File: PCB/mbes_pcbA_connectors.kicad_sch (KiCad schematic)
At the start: 15 parts

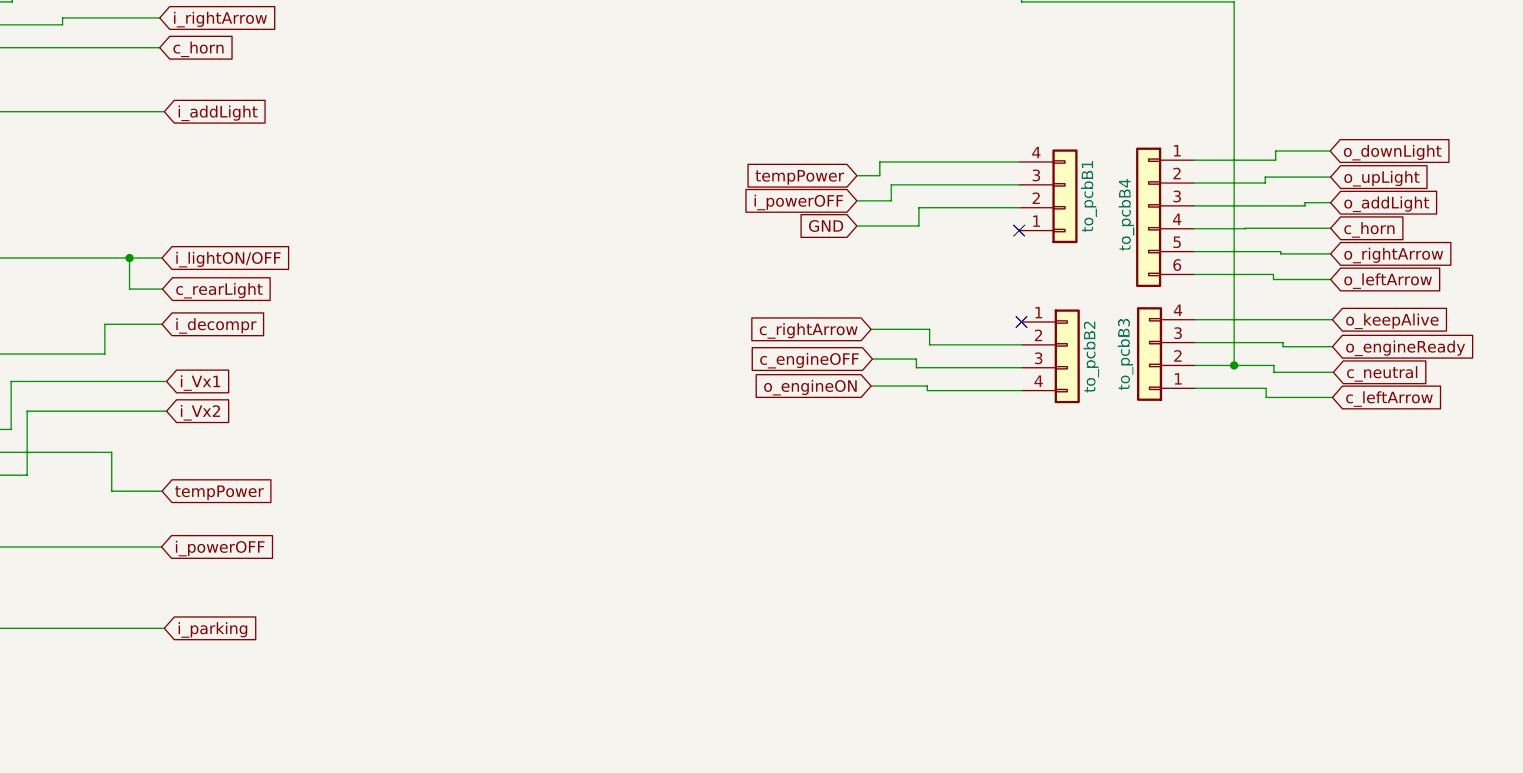
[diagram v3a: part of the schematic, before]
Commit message: No USB support and PCB-B size reducing
Implementing USB power support using 7805 was a stupid idea: too much wasted electic current in Joule effect. So, I moved just
one 7805 in the PCB-A, because the its used power is very low. It allowed me to optimize the PCB-B used space and reduce its
whole size ;-)
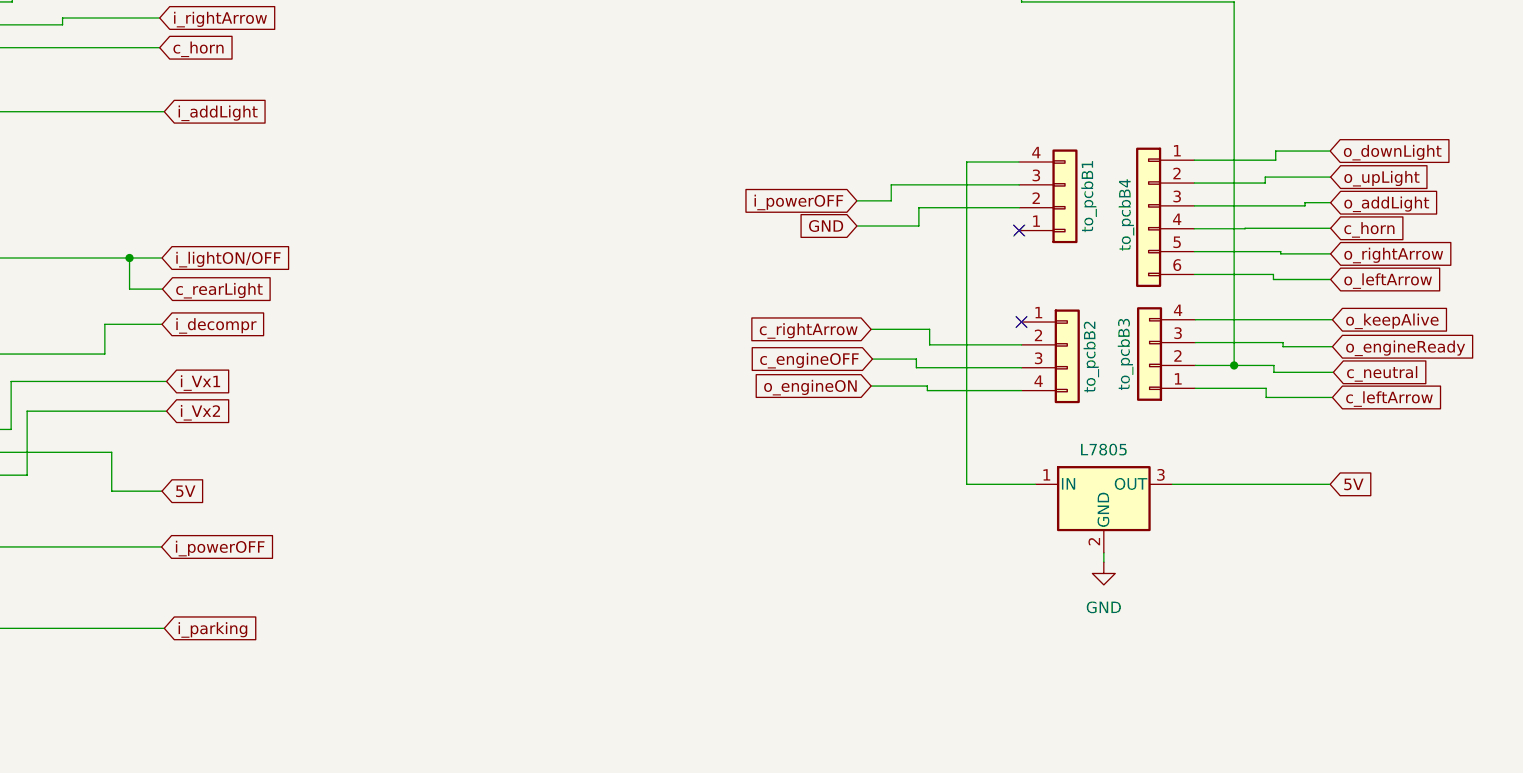
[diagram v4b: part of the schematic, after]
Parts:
- added U3: L7805, Package_TO_SOT_THT:TO-220-3_Vertical, symbol Regulator_Linear:L7805
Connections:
- net GND: now also U3.2 (GND)
- net tempPower: no longer names the net of to_pcbB1.4 (Pin_4)
- net tempPower: now also U3.1 (IN); no longer R1.1
- new net 5V: R1.1, U3.3 (OUT)

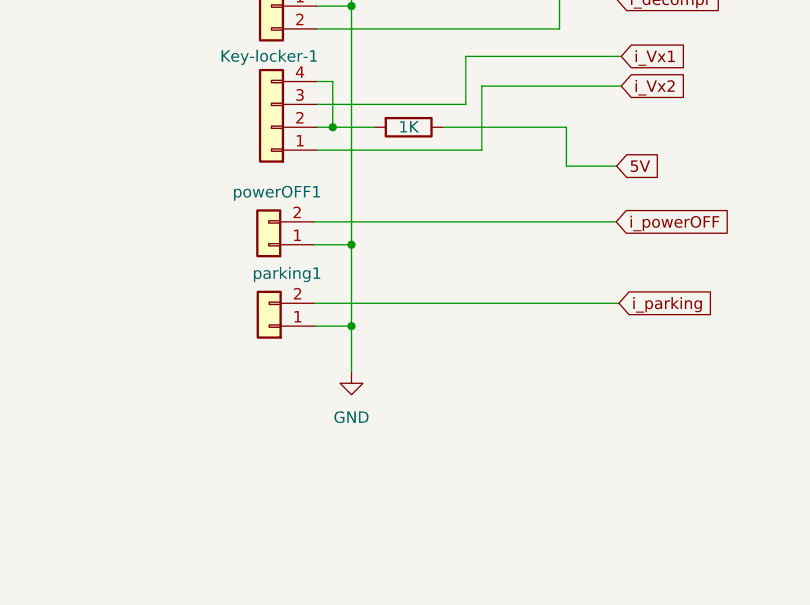
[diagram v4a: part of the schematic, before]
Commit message: External power connector, and one 100nF cap. added
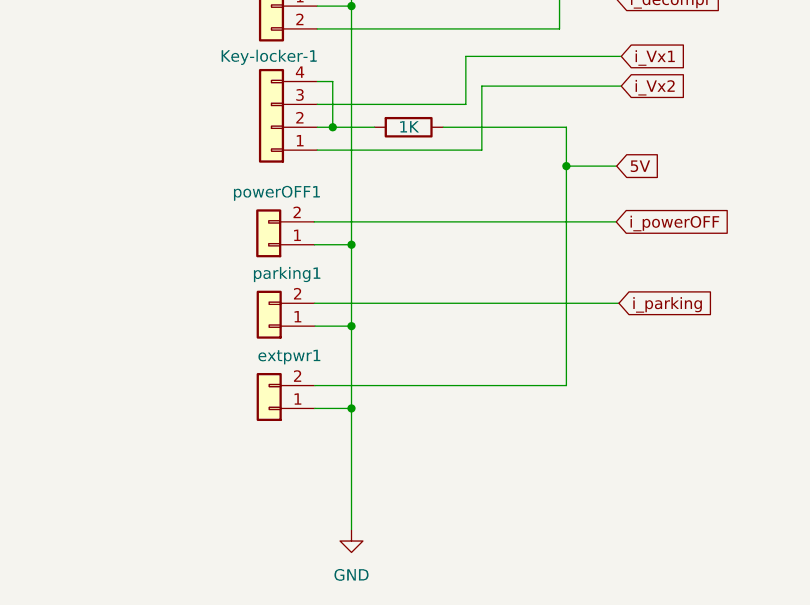
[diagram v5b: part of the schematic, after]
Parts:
- added extpwr1: Conn_01x02, Connector_PinHeader_2.54mm:PinHeader_1x02_P2.54mm_Vertical, symbol Connector_Generic:Conn_01x02
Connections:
- net 5V: now also extpwr1.2 (Pin_2)
- net GND: now also extpwr1.1 (Pin_1)
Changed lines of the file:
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@@
 	)
 	(junction
+		(at 65.786 167.132)
+		(diameter 0)
+		(color 0 0 0 0)
+	)
+	(junction
 		(at 65.786 148.9456)
 		(diameter 0)
@@
 	)
 	(junction
+		(at 89.662 140.208)
+		(diameter 0)
+		(color 0 0 0 0)
+	)
+	(junction
 		(at 91.6432 114.3)
 		(diameter 0)
@@
 	(wire
 		(pts
-			(xy 65.786 163.068) (xy 65.786 157.988)
+			(xy 65.786 180.594) (xy 65.786 167.132)
 		)
 		(stroke
@@
 	(wire
 		(pts
+			(xy 61.722 164.592) (xy 89.662 164.592)
+		)
+		(stroke
+			(width 0)
+			(type default)
+		)
+	)
+	(wire
+		(pts
 			(xy 182.88 53.848) (xy 201.549 53.848)
 		)
@@
 	(wire
 		(pts
+			(xy 89.662 164.592) (xy 89.662 140.208)
+		)
+		(stroke
+			(width 0)
+			(type default)
+		)
+	)
+	(wire
+		(pts
 			(xy 201.549 55.88) (xy 208.28 55.88)
 		)
@@
 	(wire
 		(pts
+			(xy 65.786 167.132) (xy 65.786 157.988)
+		)
+		(stroke
+			(width 0)
+			(type default)
+		)
+	)
+	(wire
+		(pts
 			(xy 176.276 106.172) (xy 190.5 106.172)
 		)
@@
 	(wire
 		(pts
+			(xy 61.722 167.132) (xy 65.786 167.132)
+		)
+		(stroke
+			(width 0)
+			(type default)
+		)
+	)
+	(wire
+		(pts
 			(xy 192.278 139.446) (xy 184.658 139.446)
 		)
@@
 	(symbol
 		(lib_id "power:GND")
-		(at 65.786 163.068 0)
+		(at 65.786 180.594 0)
 		(unit 1)
 		(exclude_from_sim no)
@@
 		(fields_autoplaced yes)
 		(property "Reference" "#PWR0108"
-			(at 65.786 169.418 0)
+			(at 65.786 186.944 0)
 			(effects
 				(font
@@
 		)
 		(property "Value" "GND"
-			(at 65.786 168.148 0)
+			(at 65.786 185.674 0)
 			(effects
 				(font
@@
 		)
 		(property "Footprint" ""
-			(at 65.786 163.068 0)
+			(at 65.786 180.594 0)
 			(effects
 				(font
@@
 		)
 		(property "Datasheet" ""
-			(at 65.786 163.068 0)
+			(at 65.786 180.594 0)
 			(effects
 				(font
@@
 		)
 		(property "Description" ""
-			(at 65.786 163.068 0)
+			(at 65.786 180.594 0)
 			(effects
 				(font
@@
 					(unit 1)
 				)
+			)
+		)
+	)
+	(symbol
+		(lib_id "Connector_Generic:Conn_01x02")
+		(at 56.642 167.132 180)
+		(unit 1)
+		(exclude_from_sim no)
+		(in_bom yes)
+		(on_board yes)
+		(dnp no)
+		(property "Reference" "extpwr1"
+			(at 62.484 161.29 0)
+			(effects
+				(font
+					(size 1.27 1.27)
+				)
+				(justify left)
+			)
+		)
+		(property "Value" "Conn_01x02"
+			(at 55.3721 169.672 90)
+			(effects
+				(font
+					(size 1.27 1.27)
+				)
+				(justify left)
+				(hide yes)
+			)
+		)
+		(property "Footprint" "Connector_PinHeader_2.54mm:PinHeader_1x02_P2.54mm_Vertical"
+			(at 56.642 167.132 0)
+			(effects
+				(font
+					(size 1.27 1.27)
+				)
+				(hide yes)
+			)
+		)
+		(property "Datasheet" "~"
+			(at 56.642 167.132 0)
+			(effects
+				(font
+					(size 1.27 1.27)
+				)
+				(hide yes)
+			)
+		)
+		(property "Description" ""
+			(at 56.642 167.132 0)
+			(effects
+				(font
+					(size 1.27 1.27)
+				)
+				(hide yes)
+			)
+		)
+		(pin "1"
+		)
+		(pin "2"
+		)
+		(instances
+			(project "pcb-a"
+				(path "/709d0967-afe5-49d3-92a5-d2bb94550bdb/0b22d592-b723-42a2-89dd-bec665c2bd26"
+					(reference "extpwr1")
+					(unit 1)
+				)
